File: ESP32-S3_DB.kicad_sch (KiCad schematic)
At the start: 0 parts

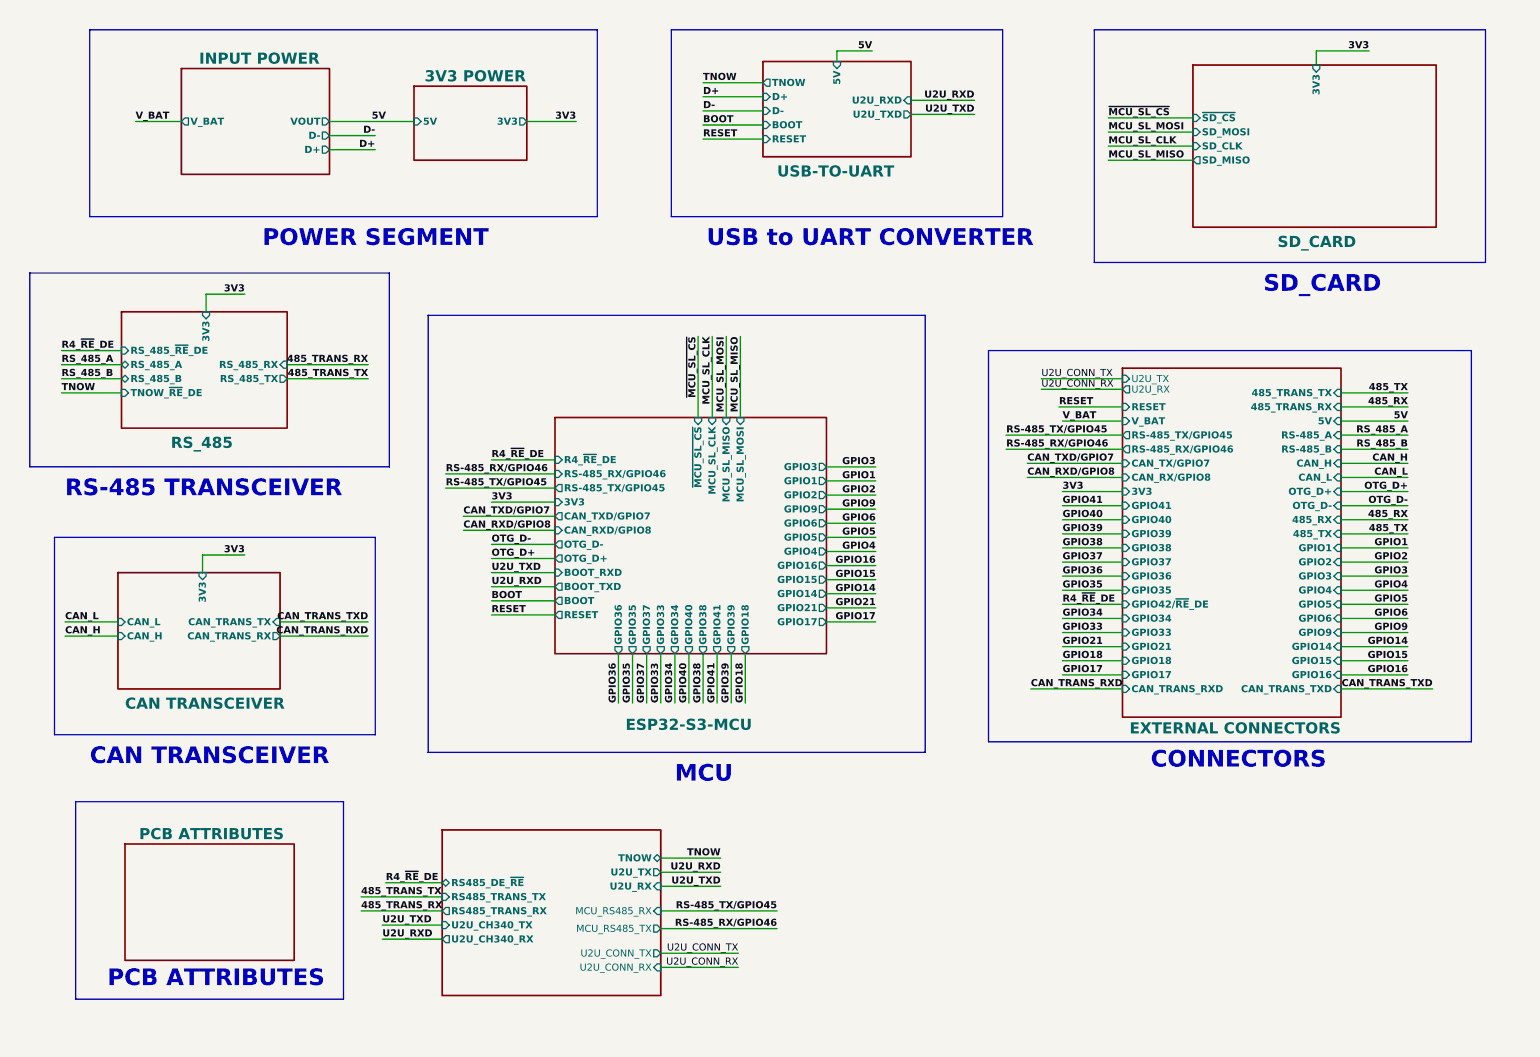
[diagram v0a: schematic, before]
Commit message: Added mounting holes
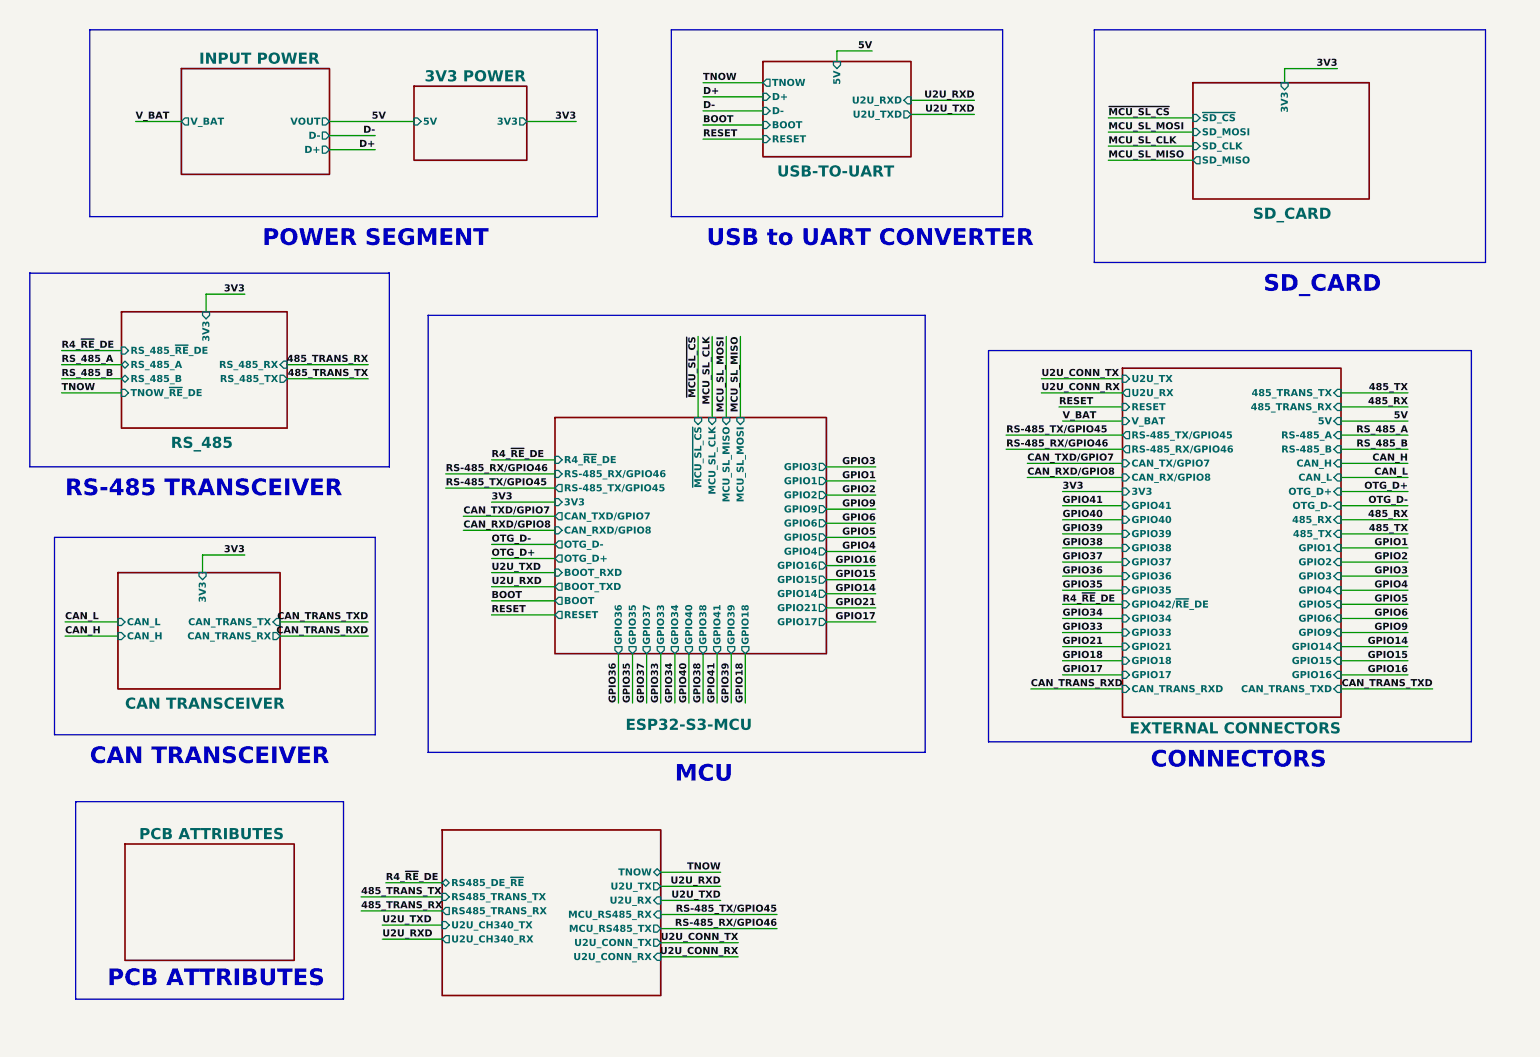
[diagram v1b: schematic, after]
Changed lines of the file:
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@@
     (stroke (width 0.5) (type default) (color 0 0 255 1))
   )
-  (wire (pts (xy 197.485 80.01) (xy 212.09 80.01))
-    (stroke (width 0) (type default))
+  (wire (pts (xy 197.485 80.645) (xy 212.09 80.645))
+    (stroke (width 0.5) (type default) (color 0 0 255 1))
   )
   (bus (pts (xy 274.955 73.025) (xy 274.955 143.51))
     (stroke (width 1) (type default) (color 72 72 72 1))
   )
-  (wire (pts (xy 128.905 173.99) (xy 149.86 173.99))
-    (stroke (width 0) (type default))
+  (wire (pts (xy 128.905 174.625) (xy 149.86 174.625))
+    (stroke (width 0.5) (type default) (color 0 0 255 1))
   )
   (wire (pts (xy 144.145 127.635) (xy 144.145 136.525))
@@
     (stroke (width 0.5) (type default) (color 72 0 72 1))
   )
-  (wire (pts (xy 128.905 167.005) (xy 139.7 167.005))
+  (wire (pts (xy 128.905 169.545) (xy 139.7 169.545))
     (stroke (width 0.5) (type default) (color 0 0 255 1))
   )
@@
   )
   (wire (pts (xy 197.485 78.105) (xy 212.09 78.105))
-    (stroke (width 0) (type default))
+    (stroke (width 0.5) (type default) (color 0 0 255 1))
   )
   (wire (pts (xy 98.425 107.95) (xy 109.855 107.95))
@@
     (stroke (width 1) (type default) (color 72 72 72 1))
   )
-  (wire (pts (xy 128.905 181.61) (xy 142.875 181.61))
-    (stroke (width 0) (type default))
+  (wire (pts (xy 128.905 179.705) (xy 142.875 179.705))
+    (stroke (width 0.5) (type default) (color 0 0 255 1))
   )
   (wire (pts (xy 212.09 108.585) (xy 201.295 108.585))
@@
     (stroke (width 1) (type default) (color 72 72 72 1))
   )
-  (wire (pts (xy 128.905 169.545) (xy 139.7 169.545))
+  (wire (pts (xy 128.905 172.085) (xy 139.7 172.085))
     (stroke (width 0.5) (type default) (color 0 0 255 1))
   )
@@
     (stroke (width 0.5) (type default) (color 72 0 72 1))
   )
-  (wire (pts (xy 128.905 164.465) (xy 139.7 164.465))
+  (wire (pts (xy 128.905 167.005) (xy 139.7 167.005))
     (stroke (width 0.5) (type default) (color 0 194 0 1))
   )
-  (wire (pts (xy 247.015 19.05) (xy 247.015 21.59))
+  (wire (pts (xy 241.3 22.225) (xy 241.3 24.765))
     (stroke (width 0.5) (type default) (color 255 0 0 1))
   )
@@
   )
   (wire (pts (xy 128.905 177.165) (xy 149.86 177.165))
-    (stroke (width 0) (type default))
+    (stroke (width 0.5) (type default) (color 0 0 255 1))
   )
   (wire (pts (xy 251.46 106.045) (xy 263.525 106.045))
@@
     (stroke (width 0.5) (type default) (color 255 0 0 1))
   )
-  (wire (pts (xy 247.015 19.05) (xy 256.54 19.05))
+  (wire (pts (xy 241.3 22.225) (xy 250.825 22.225))
     (stroke (width 0.5) (type default) (color 255 0 0 1))
   )
@@
     (stroke (width 1) (type default) (color 72 72 72 1))
   )
-  (wire (pts (xy 128.905 184.15) (xy 142.875 184.15))
-    (stroke (width 0) (type default))
+  (wire (pts (xy 128.905 182.245) (xy 142.875 182.245))
+    (stroke (width 0.5) (type default) (color 0 0 255 1))
   )
   (wire (pts (xy 78.74 176.53) (xy 89.535 176.53))
@@
     (effects (font (size 1.27 1.27) bold (color 72 0 72 1)) (justify left bottom))
   )
-  (label "3V3" (at 256.54 19.05 180) (fields_autoplaced)
+  (label "3V3" (at 250.825 22.225 180) (fields_autoplaced)
     (effects (font (size 1.27 1.27) bold (color 255 0 0 1)) (justify right bottom))
   )
@@
     (effects (font (size 1.27 1.27) bold (color 0 0 255 1)) (justify left bottom))
   )
-  (label "U2U_CONN_RX" (at 142.875 184.15 180) (fields_autoplaced)
-    (effects (font (size 1.27 1.27)) (justify right bottom))
+  (label "U2U_CONN_RX" (at 142.875 182.245 180) (fields_autoplaced)
+    (effects (font (size 1.27 1.27) (thickness 0.254) bold (color 0 0 255 1)) (justify right bottom))
   )
   (label "CAN_RXD{slash}GPIO8" (at 194.945 95.885 0) (fields_autoplaced)
@@
     (effects (font (size 1.27 1.27) bold (color 72 0 72 1)) (justify right bottom))
   )
-  (label "U2U_RXD" (at 139.7 167.005 180) (fields_autoplaced)
+  (label "U2U_RXD" (at 139.7 169.545 180) (fields_autoplaced)
     (effects (font (size 1.27 1.27) bold (color 0 0 255 1)) (justify right bottom))
   )
@@
     (effects (font (size 1.27 1.27) bold (color 0 0 255 1)) (justify right bottom))
   )
-  (label "TNOW" (at 139.7 164.465 180) (fields_autoplaced)
+  (label "TNOW" (at 139.7 167.005 180) (fields_autoplaced)
     (effects (font (size 1.27 1.27) bold (color 0 194 0 1)) (justify right bottom))
   )
@@
     (effects (font (size 1.27 1.27) bold (color 0 0 255 1)) (justify left bottom))
   )
-  (label "RS-485_TX{slash}GPIO45" (at 149.86 173.99 180) (fields_autoplaced)
+  (label "RS-485_TX{slash}GPIO45" (at 149.86 174.625 180) (fields_autoplaced)
     (effects (font (size 1.27 1.27) bold (color 0 0 255 1)) (justify right bottom))
   )
@@
   )
   (label "U2U_CONN_TX" (at 197.485 78.105 0) (fields_autoplaced)
-    (effects (font (size 1.27 1.27)) (justify left bottom))
+    (effects (font (size 1.27 1.27) (thickness 0.254) bold (color 0 0 255 1)) (justify left bottom))
   )
   (label "485_RX" (at 263.525 83.185 180) (fields_autoplaced)
@@
     (effects (font (size 1.27 1.27) bold (color 72 0 72 1)) (justify right bottom))
   )
-  (label "U2U_CONN_TX" (at 142.875 181.61 180) (fields_autoplaced)
-    (effects (font (size 1.27 1.27)) (justify right bottom))
+  (label "U2U_CONN_TX" (at 142.875 179.705 180) (fields_autoplaced)
+    (effects (font (size 1.27 1.27) (thickness 0.254) bold (color 0 0 255 1)) (justify right bottom))
   )
   (label "GPIO6" (at 167.64 104.14 180) (fields_autoplaced)
@@
     (effects (font (size 1.27 1.27) bold (color 0 0 255 1)) (justify left bottom))
   )
-  (label "U2U_CONN_RX" (at 197.485 80.01 0) (fields_autoplaced)
-    (effects (font (size 1.27 1.27)) (justify left bottom))
+  (label "U2U_CONN_RX" (at 197.485 80.645 0) (fields_autoplaced)
+    (effects (font (size 1.27 1.27) (thickness 0.254) bold (color 0 0 255 1)) (justify left bottom))
   )
   (label "TNOW" (at 136.525 24.765 0) (fields_autoplaced)
@@
     (effects (font (size 1.27 1.27) bold (color 72 0 72 1)) (justify left bottom))
   )
-  (label "U2U_TXD" (at 139.7 169.545 180) (fields_autoplaced)
+  (label "U2U_TXD" (at 139.7 172.085 180) (fields_autoplaced)
     (effects (font (size 1.27 1.27) bold (color 0 0 255 1)) (justify right bottom))
   )
@@
     (effects (font (size 1.27 1.27) bold (color 0 0 0 1)) (justify left bottom))
   )
-  (sheet (at 224.79 21.59) (size 43.815 29.21)
+  (sheet (at 224.79 24.765) (size 31.75 20.955)
     (stroke (width 0.3) (type solid) (color 0 0 0 1))
     (fill (color 255 255 194 1.0000))
-    (property "Sheetname" "SD_CARD" (at 240.03 54.61 0)
+    (property "Sheetname" "SD_CARD" (at 235.585 49.53 0)
       (effects (font (size 2 2) bold (color 0 0 0 1)) (justify left bottom))
     )
-    (property "Sheetfile" "SD_Card.kicad_sch" (at 224.79 51.3846 0)
+    (property "Sheetfile" "SD_Card.kicad_sch" (at 224.79 54.5596 0)
       (effects (font (size 1.27 1.27)) (justify left top) hide)
     )
@@
       (effects (font (size 1.27 1.27) (thickness 0.254) bold (color 204 102 0 1)) (justify left))
     )
-    (pin "3V3" input (at 247.015 21.59 90)
+    (pin "3V3" input (at 241.3 24.765 90)
       (effects (font (size 1.27 1.27) (thickness 0.254) bold (color 255 0 0 1)) (justify right))
     )
@@
     )
     (pin "U2U_TX" input (at 212.09 78.105 180)
-      (effects (font (size 1.27 1.27)) (justify left))
-    )
-    (pin "U2U_RX" output (at 212.09 80.01 180)
-      (effects (font (size 1.27 1.27)) (justify left))
+      (effects (font (size 1.27 1.27) (thickness 0.254) bold (color 0 0 255 1)) (justify left))
+    )
+    (pin "U2U_RX" output (at 212.09 80.645 180)
+      (effects (font (size 1.27 1.27) (thickness 0.254) bold (color 0 0 255 1)) (justify left))
     )
     (instances
@@
       (effects (font (size 1.27 1.27) (thickness 0.254) bold (color 0 194 0 1)) (justify left))
     )
-    (pin "TNOW" bidirectional (at 128.905 164.465 0)
+    (pin "TNOW" bidirectional (at 128.905 167.005 0)
       (effects (font (size 1.27 1.27) (thickness 0.254) bold (color 0 194 0 1)) (justify right))
     )
-    (pin "U2U_CONN_TX" output (at 128.905 181.61 0)
-      (effects (font (size 1.27 1.27)) (justify right))
-    )
-    (pin "U2U_CONN_RX" input (at 128.905 184.15 0)
-      (effects (font (size 1.27 1.27)) (justify right))
-    )
-    (pin "MCU_RS485_RX" input (at 128.905 173.99 0)
-      (effects (font (size 1.27 1.27)) (justify right))
+    (pin "U2U_CONN_TX" output (at 128.905 179.705 0)
+      (effects (font (size 1.27 1.27) (thickness 0.254) bold (color 0 0 255 1)) (justify right))
+    )
+    (pin "U2U_CONN_RX" input (at 128.905 182.245 0)
+      (effects (font (size 1.27 1.27) (thickness 0.254) bold (color 0 0 255 1)) (justify right))
+    )
+    (pin "MCU_RS485_RX" input (at 128.905 174.625 0)
+      (effects (font (size 1.27 1.27) (thickness 0.254) bold (color 0 0 255 1)) (justify right))
     )
     (pin "MCU_RS485_TX" output (at 128.905 177.165 0)
-      (effects (font (size 1.27 1.27)) (justify right))
+      (effects (font (size 1.27 1.27) (thickness 0.254) bold (color 0 0 255 1)) (justify right))
     )
     (pin "RS485_TRANS_TX" input (at 89.535 171.45 180)
       (effects (font (size 1.27 1.27) (thickness 0.254) bold (color 0 0 255 1)) (justify left))
     )
-    (pin "U2U_TX" output (at 128.905 167.005 0)
+    (pin "U2U_TX" output (at 128.905 169.545 0)
       (effects (font (size 1.27 1.27) (thickness 0.254) bold (color 0 0 255 1)) (justify right))
     )
@@
       (effects (font (size 1.27 1.27) (thickness 0.254) bold (color 0 0 255 1)) (justify left))
     )
-    (pin "U2U_RX" input (at 128.905 169.545 0)
-      (effects (font (size 1.27 1.27) (thickness 0.254) bold (color 0 0 255 1)) (justify right))
-    )
+    (pin "U2U_RX" input (at 128.905 172.085 0)
+      (effects (font (size 1.27 1.27) (thickness 0.254) bold (color 0 0 255 1)) (justify right))
+    )

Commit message: Made changes in schematics, changed hierarchical sheet color
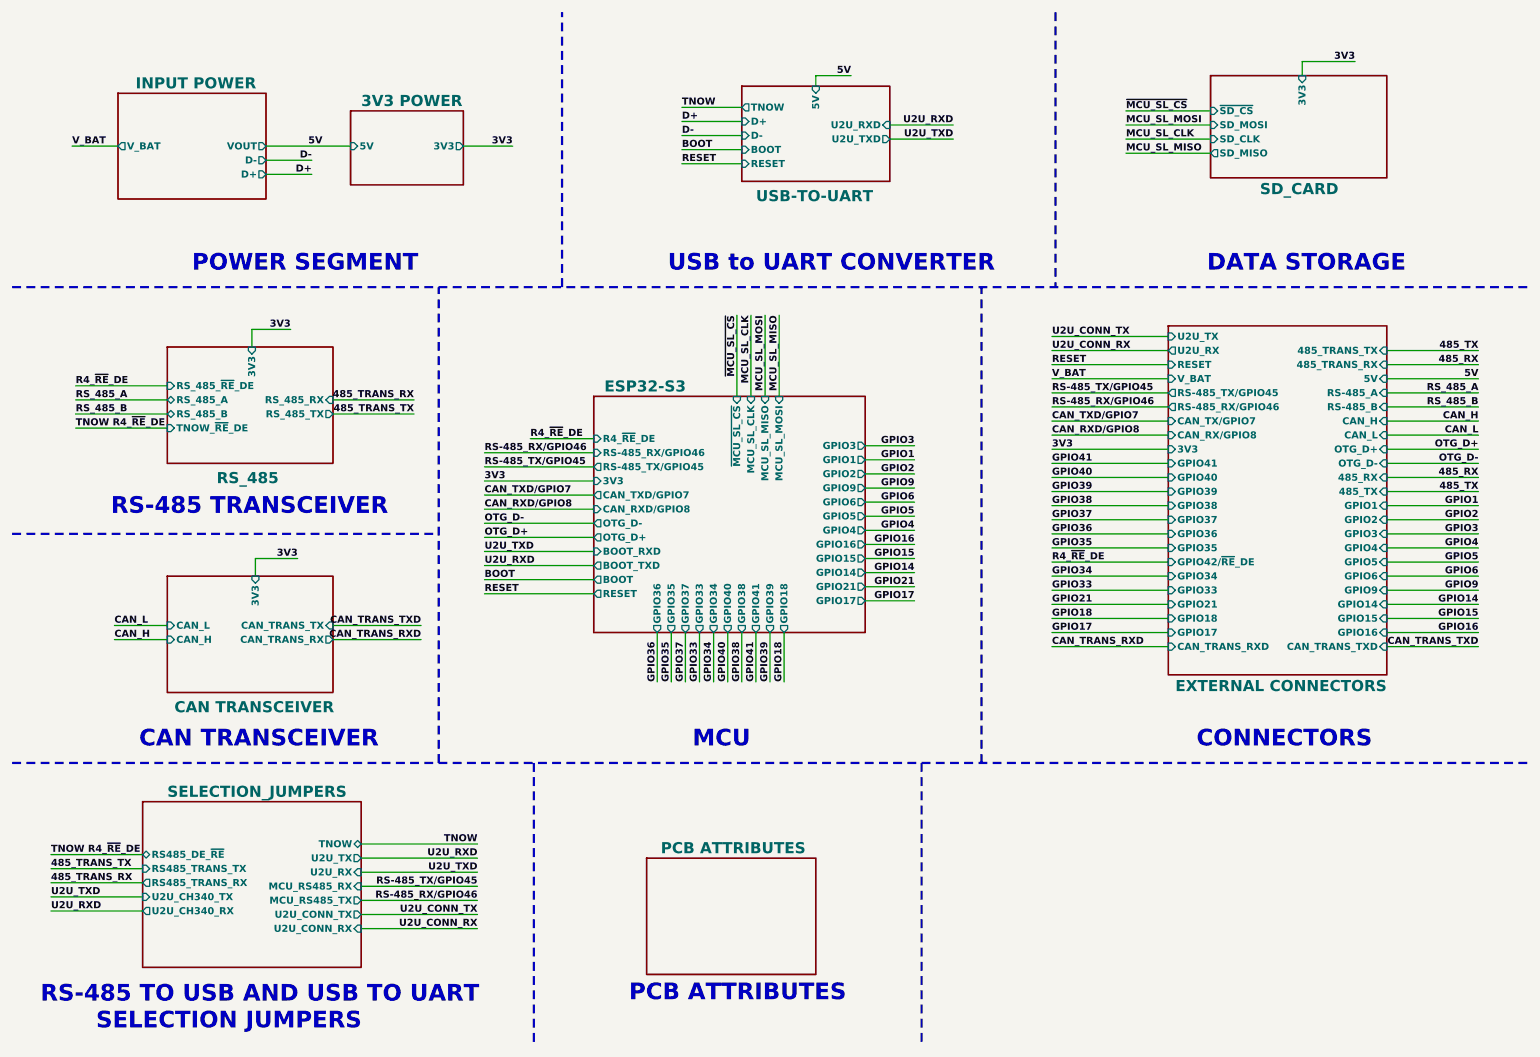
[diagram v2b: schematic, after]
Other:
- sheet ESP32-S3-MCU renamed ESP32-S3
- sheet Selection_jumpers renamed SELECTION_JUMPERS
- note added: "DATA STORAGE"
- note added: "RS-485 TO USB AND USB TO UART SELECTION JUMPERS"
- note removed: "SD_CARD"

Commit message: Instigated routing
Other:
- title: (none) -> HARDWARE TINKERERS ESP32-S3 DB
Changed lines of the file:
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@@
 (kicad_sch (version 20230121) (generator eeschema)
   (paper "A4")
+  (title_block
+    (title "HARDWARE TINKERERS ESP32-S3 DB")
+    (rev "1.0.0")
+  )
   (wire (pts (xy 143.51 39.37) (xy 132.715 39.37))
     (stroke (width 0.5) (type default) (color 0 194 0 1))
